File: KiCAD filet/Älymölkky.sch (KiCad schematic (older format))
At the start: 6 parts

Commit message: Added lots of new reference files and a new lib
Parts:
- removed U?: nRF52810-QCxx, Package_DFN_QFN:QFN-32-1EP_5x5mm_P0.5mm_EP3.6x3.6mm, symbol MCU_Nordic:nRF52810-QCxx
- added DEC1_C4, Vdd_nRF_C5: 100nF, symbol Device:C
- added L?: L, symbol Device:L
- added U?: nRF52810-QCxx, Package_DFN_QFN:QFN-32-1EP_5x5mm_P0.5mm_EP3.6x3.6mm, symbol MCU_Nordic_modified:nRF52810-QCxx
- added Vdd_nRF_C9: 4.7uF, symbol Device:C
- renumbered Vdd_nRF_C to Vdd_nRF_C8
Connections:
- net labels added: ANTENNA, LIS_INT1, VDD, ~CS, ~INT1, ~INT2, ~SAO_SDO, ~SCL_SPC, ~SDA_SDI
- net labels removed: Power_input_3.3V, Vdd, Vdd_IO, Vdd_nRF_input
- wire segments 37 -> 51
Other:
- note added: "Pin 32 to C9\nPin 25 to C8\nPin 9 to C5"
- moved on the sheet: Vdd_nRF_C8
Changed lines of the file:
@@
 EESchema Schematic File Version 4
+LIBS:Älymölkky-cache
 EELAYER 26 0
 EELAYER END
@@
 Wire Wire Line
 	7650 4750 7650 3350
-Text GLabel 8100 2750 0    50   Input ~ 0
-Power_input_3.3V
-Wire Wire Line
-	8250 2750 8100 2750
 Wire Wire Line
 	7650 3350 7950 3350
-Text Label 7950 3150 0    50   ~ 0
-Vdd_IO
 Wire Wire Line
 	7950 3000 8250 3000
@@
 Connection ~ 8950 4700
 Wire Wire Line
-	8950 4700 8950 5750
+	8950 4700 8950 5550
 Wire Wire Line
 	8200 4200 8200 3600
-Wire Wire Line
-	8200 3600 8500 3600
 Wire Wire Line
 	8500 3600 8500 2750
@@
 Connection ~ 8200 4200
 Connection ~ 8250 2750
-Text Label 8300 3600 0    50   ~ 0
-Vdd
-$Comp
-L MCU_Nordic:nRF52810-QCxx U?
-U 1 1 5C5B485F
-P 2850 5100
-F 0 "U?" H 2850 4014 50  0000 C CNN
-F 1 "nRF52810-QCxx" H 2850 3923 50  0000 C CNN
-F 2 "Package_DFN_QFN:QFN-32-1EP_5x5mm_P0.5mm_EP3.6x3.6mm" H 2850 3750 50  0001 C CNN
-F 3 "http://infocenter.nordicsemi.com/pdf/nRF52810_PS_v1.1.pdf" H 2350 5300 50  0001 C CNN
-	1    2850 5100
-	1    0    0    -1
-$EndComp
-$Comp
-L Device:C Vdd_nRF_C
+$Comp
+L Device:C Vdd_nRF_C8
 U 1 1 5C5B4866
-P 3250 3050
-F 0 "Vdd_nRF_C" H 3365 3096 50  0000 L CNN
-F 1 "100nF" H 3365 3005 50  0000 L CNN
-F 2 "" H 3250 3050 50  0001 C CNN
-F 3 "~" H 3250 3050 50  0001 C CNN
-	1    3250 3050
-	1    0    0    -1
-$EndComp
-Wire Wire Line
-	2850 4100 2850 2700
-Wire Wire Line
-	2850 2700 3100 2700
-$Comp
-L power:Earth #PWR?
-U 1 1 5C5B4870
-P 3250 3350
-F 0 "#PWR?" H 3250 3100 50  0001 C CNN
-F 1 "Earth" H 3250 3200 50  0001 C CNN
-F 2 "" H 3250 3350 50  0001 C CNN
-F 3 "~" H 3250 3350 50  0001 C CNN
-	1    3250 3350
-	1    0    0    -1
-$EndComp
-Text GLabel 3000 2300 0    50   Input ~ 0
-Vdd_nRF_input
-Wire Wire Line
-	3100 2700 3100 2300
-Wire Wire Line
-	3100 2300 3000 2300
-Connection ~ 3100 2700
-Wire Wire Line
-	3100 2700 3250 2700
+P 5200 3000
+F 0 "Vdd_nRF_C8" H 5315 3046 39  0000 L CNN
+F 1 "100nF" H 5315 2955 50  0000 L CNN
+F 2 "" H 5200 3000 50  0001 C CNN
+F 3 "~" H 5200 3000 50  0001 C CNN
+	1    5200 3000
+	1    0    0    -1
+$EndComp
 Wire Wire Line
 	8300 4200 8200 4200
@@
 Wire Wire Line
 	8950 3350 8950 3700
-Wire Wire Line
-	3250 2700 3250 2900
-Wire Wire Line
-	3250 3200 3250 3350
+Text Label 6750 6100 0    50   ~ 0
+LIS_INT1
+Text Label 7150 5050 2    50   ~ 0
+~CS
+Text Label 5950 4950 0    50   ~ 0
+~CS
+$Comp
+L Device:L L?
+U 1 1 5C5CAB8B
+P 6650 3900
+F 0 "L?" H 6703 3946 50  0000 L CNN
+F 1 "L" H 6703 3855 50  0000 L CNN
+F 2 "" H 6650 3900 50  0001 C CNN
+F 3 "~" H 6650 3900 50  0001 C CNN
+	1    6650 3900
+	1    0    0    -1
+$EndComp
+Wire Wire Line
+	5950 4600 5950 4550
+Wire Wire Line
+	6650 3750 6650 3600
+Text Label 6650 3600 0    50   ~ 0
+ANTENNA
+Wire Wire Line
+	8100 2750 8250 2750
+Wire Wire Line
+	8500 3600 8200 3600
+Text Label 7150 5150 2    50   ~ 0
+~SDA_SDI
+Text Label 5950 5050 0    50   ~ 0
+~SDA_SDI
+Text Label 7150 5250 2    50   ~ 0
+~SAO_SDO
+Text Label 5950 5150 0    50   ~ 0
+~SAO_SDO
+Text Label 7150 5350 2    50   ~ 0
+~SCL_SPC
+Text Label 5950 5250 0    50   ~ 0
+~SCL_SPC
+Text Label 8050 5150 0    50   ~ 0
+~INT1
+Text Label 5950 5450 0    50   ~ 0
+~INT1
+Text Label 8050 5250 0    50   ~ 0
+~INT2
+Text Label 5950 5550 0    50   ~ 0
+~INT2
+Wire Wire Line
+	8050 5550 8950 5550
+Connection ~ 8950 5550
+Wire Wire Line
+	8950 5550 8950 5750
+$Comp
+L Device:C Vdd_nRF_C9
+U 1 1 5C5D0DD8
+P 5800 3000
+F 0 "Vdd_nRF_C9" H 5915 3046 39  0000 L CNN
+F 1 "4.7uF" H 5915 2955 50  0000 L CNN
+F 2 "" H 5800 3000 50  0001 C CNN
+F 3 "~" H 5800 3000 50  0001 C CNN
+	1    5800 3000
+	1    0    0    -1
+$EndComp
+$Comp
+L Device:C Vdd_nRF_C5
+U 1 1 5C5D0E00
+P 6400 3000
+F 0 "Vdd_nRF_C5" H 6515 3046 39  0000 L CNN
+F 1 "100nF" H 6515 2955 50  0000 L CNN
+F 2 "" H 6400 3000 50  0001 C CNN
+F 3 "~" H 6400 3000 50  0001 C CNN
+	1    6400 3000
+	1    0    0    -1
+$EndComp
+Wire Wire Line
+	6650 4050 6650 4600
+Wire Wire Line
+	5950 4600 6650 4600
+Wire Wire Line
+	4550 4250 4550 3400
+Wire Wire Line
+	4550 3400 3750 3400
+Wire Wire Line
+	3750 3400 3750 3650
+$Comp
+L Device:C DEC1_C4
+U 1 1 5C5D43A2
+P 3750 3800
+F 0 "DEC1_C4" H 3865 3846 50  0000 L CNN
+F 1 "100nF" H 3865 3755 50  0000 L CNN
+F 2 "" H 3788 3650 50  0001 C CNN
+F 3 "~" H 3750 3800 50  0001 C CNN
+	1    3750 3800
+	1    0    0    -1
+$EndComp
+$Comp
+L power:VDD #PWR?
+U 1 1 5C5D4AF2
+P 5200 2800
+F 0 "#PWR?" H 5200 2650 50  0001 C CNN
+F 1 "VDD" H 5217 2973 50  0000 C CNN
+F 2 "" H 5200 2800 50  0001 C CNN
+F 3 "" H 5200 2800 50  0001 C CNN
+	1    5200 2800
+	1    0    0    -1
+$EndComp
+$Comp
+L power:VDD #PWR?
+U 1 1 5C5D4F0A
+P 8100 2750
+F 0 "#PWR?" H 8100 2600 50  0001 C CNN
+F 1 "VDD" H 8117 2923 50  0000 C CNN
+F 2 "" H 8100 2750 50  0001 C CNN
+F 3 "" H 8100 2750 50  0001 C CNN
+	1    8100 2750
+	1    0    0    -1
+$EndComp
+$Comp
+L power:Earth #PWR?
+U 1 1 5C5D52FB
+P 3750 3950
+F 0 "#PWR?" H 3750 3700 50  0001 C CNN
+F 1 "Earth" H 3750 3800 50  0001 C CNN
+F 2 "" H 3750 3950 50  0001 C CNN
+F 3 "~" H 3750 3950 50  0001 C CNN
+	1    3750 3950
+	1    0    0    -1
+$EndComp
+$Comp
+L MCU_Nordic_modified:nRF52810-QCxx U?
+U 1 1 5C5D854C
+P 5050 5250
+F 0 "U?" H 5050 4164 50  0000 C CNN
+F 1 "nRF52810-QCxx" H 5050 4073 50  0000 C CNN
+F 2 "Package_DFN_QFN:QFN-32-1EP_5x5mm_P0.5mm_EP3.6x3.6mm" H 5050 3900 50  0001 C CNN
+F 3 "http://infocenter.nordicsemi.com/pdf/nRF52810_PS_v1.1.pdf" H 4550 5450 50  0001 C CNN
+	1    5050 5250
+	1    0    0    -1
+$EndComp
+$Comp
+L power:Earth #PWR?
+U 1 1 5C5DA614
+P 5200 3150
+F 0 "#PWR?" H 5200 2900 50  0001 C CNN
+F 1 "Earth" H 5200 3000 50  0001 C CNN
+F 2 "" H 5200 3150 50  0001 C CNN
+F 3 "~" H 5200 3150 50  0001 C CNN
+	1    5200 3150
+	1    0    0    -1
+$EndComp
+Wire Wire Line
+	5050 2800 5200 2800
+Wire Wire Line
+	5200 2800 5200 2850
+Text Notes 6150 2400 0    50   ~ 0
+Pin 32 to C9\nPin 25 to C8\nPin 9 to C5
+Wire Wire Line
+	5250 4250 5250 3300
+Wire Wire Line
+	5250 3300 5700 3300
+Wire Wire Line
+	5700 3300 5700 2800
+Wire Wire Line
+	5700 2800 5800 2800
+Wire Wire Line
+	5800 2800 5800 2850
+Wire Wire Line
+	5350 4250 5350 3350
+Wire Wire Line
+	5350 3350 6300 3350
+Wire Wire Line
+	6300 3350 6300 2850
+Wire Wire Line
+	6300 2850 6400 2850
+Connection ~ 5200 2800
+$Comp
+L power:VDD #PWR?
+U 1 1 5C5DDF92
+P 5800 2800
+F 0 "#PWR?" H 5800 2650 50  0001 C CNN
+F 1 "VDD" H 5817 2973 50  0000 C CNN
+F 2 "" H 5800 2800 50  0001 C CNN
+F 3 "" H 5800 2800 50  0001 C CNN
+	1    5800 2800
+	1    0    0    -1
+$EndComp
+Connection ~ 5800 2800
+$Comp
+L power:VDD #PWR?
+U 1 1 5C5DDFD9
+P 6400 2850
+F 0 "#PWR?" H 6400 2700 50  0001 C CNN
+F 1 "VDD" H 6417 3023 50  0000 C CNN
+F 2 "" H 6400 2850 50  0001 C CNN
+F 3 "" H 6400 2850 50  0001 C CNN
+	1    6400 2850
+	1    0    0    -1
+$EndComp
+Connection ~ 6400 2850
+Wire Wire Line
+	5050 2800 5050 4300
 $EndSCHEMATC

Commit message: Removed redundant files and more cleanup
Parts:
- U?: symbol MCU_Nordic_modified:nRF52810-QCxx -> nrf52810-qcxx:nRF52810-QCxx
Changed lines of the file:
@@
 EESchema Schematic File Version 4
-LIBS:Älymölkky-cache
 EELAYER 26 0
 EELAYER END
@@
 $EndComp
 $Comp
-L MCU_Nordic_modified:nRF52810-QCxx U?
+L nrf52810-qcxx:nRF52810-QCxx U?
 U 1 1 5C5D854C
 P 5050 5250

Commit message: Added most of nrf52 pin connections
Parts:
- added DEC2_C6: N.C., symbol Device:C
- added DEC3_C7: 100pF, symbol Device:C
- added DEC4_C10: 1.0uF, symbol Device:C
- added U?: nRF52810-QCxx, Package_DFN_QFN:QFN-32-1EP_5x5mm_P0.5mm_EP3.6x3.6mm, symbol MCU_Nordic:nRF52810-QCxx
- added VSS_PIN20_C3: 0.8pF, symbol Device:C
- added X1, X2: 32MHz Crystal, symbol Device:Crystal
- added XC1_C1, XC2_C2, XL1_C11, XL2_C12: 12pF, symbol Device:C
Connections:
- net labels added: ~Reset, ~SWDCLK, ~SWDIO, ~VSS_PIN20
- net labels removed: LIS_INT1
- wire segments 51 -> 100
- no-connect marks 0 -> 8
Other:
- note added: "AIN0-AIN6+VDD/2 are multiplexer pins"
- note added: "OPTIONAL"
- note added: "Pin 29 (VSS) to DEC4 ground"
- moved on the sheet: L?

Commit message: Added comments on some pins
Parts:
- X2: value 32MHz Crystal -> 32.768 kHz Crystal
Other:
- note added: "For LIS2DE12:\nThe device core is supplied through the Vdd line\nwhile the I/O pads are supplied through the Vdd_IO line. \nPower supply decoupling capacitors (100 nF ceramic,\n 10 μF aluminum) should be placed as near as possible to\npin 9 of the device (common design practice).\n"
- note added: "Placeholder for antenna"
- note added: "SWDCLK and SWDIO are serial wire debug ports"
- note added: "VDD pins:\nPin 32 to C9\nPin 25 to C8\nPin 9 to C5"
- note added: "VSS pins:\nPin 20 to antenna ground\nPin 29 and 33 passive."
- note removed: "For LIS2DE12:\nThe device core is supplied through the Vdd line while the I/O pads are supplied through the\nVdd_IO line. Power supply decoupling capacitors (100 nF ceramic, 10 μF aluminum) should\nbe placed as near as possible to pin 9 of the device (common design practice).\n"
- note removed: "Pin 32 to C9\nPin 25 to C8\nPin 9 to C5"
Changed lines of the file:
@@
 $EndComp
 Text Notes 8950 2900 0    50   ~ 0
-For LIS2DE12:\nThe device core is supplied through the Vdd line while the I/O pads are supplied through the\nVdd_IO line. Power supply decoupling capacitors (100 nF ceramic, 10 μF aluminum) should\nbe placed as near as possible to pin 9 of the device (common design practice).\n
+For LIS2DE12:\nThe device core is supplied through the Vdd line\nwhile the I/O pads are supplied through the Vdd_IO line. \nPower supply decoupling capacitors (100 nF ceramic,\n 10 μF aluminum) should be placed as near as possible to\npin 9 of the device (common design practice).\n
 Wire Wire Line
 	7650 4750 7650 3350
@@
 Wire Wire Line
 	5200 2800 5200 2850
-Text Notes 6150 2400 0    50   ~ 0
-Pin 32 to C9\nPin 25 to C8\nPin 9 to C5
+Text Notes 5900 2550 0    50   ~ 0
+VDD pins:\nPin 32 to C9\nPin 25 to C8\nPin 9 to C5
 Wire Wire Line
 	5250 4250 5250 4050
@@
 	1    0    0    -1
 $EndComp
-Text Notes 5050 2100 0    50   ~ 0
+Text Notes 4950 2000 0    50   ~ 0
 Pin 29 (VSS) to DEC4 ground
 $Comp
@@
 P 6200 4000
 F 0 "X2" V 6154 4131 50  0000 L TNN
-F 1 "32MHz Crystal" V 6245 4131 50  0000 L CNN
+F 1 "32.768 kHz Crystal" V 6245 4131 50  0000 L CNN
 F 2 "" H 6200 4000 50  0001 C CNN
 F 3 "~" H 6200 4000 50  0001 C CNN
@@
 Text Label 3800 4650 0    50   ~ 0
 ~VSS_PIN20
-Text Label 5450 6350 0    50   ~ 0
+Text Label 5050 6050 0    50   ~ 0
 ~VSS_PIN20
 Wire Wire Line
@@
 NoConn ~ 5950 5350
 NoConn ~ 5950 5650
-Text Notes 6100 5800 0    39   ~ 0
+Text Notes 6050 5800 0    39   ~ 0
 AIN0-AIN6+VDD/2 are multiplexer pins
 NoConn ~ 5950 5750
@@
 $EndComp
 Connection ~ 6400 2800
+Text Notes 2950 6100 0    50   ~ 0
+SWDCLK and SWDIO are serial wire debug ports
+Text Notes 2500 4250 0    50   ~ 0
+Placeholder for antenna
+Text Notes 5450 6300 0    50   ~ 0
+VSS pins:\nPin 20 to antenna ground\nPin 29 and 33 passive.
 $EndSCHEMATC

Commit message: Added test points, leds and serial port programming pins
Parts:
- removed U?: nRF52810-QCxx, Package_DFN_QFN:QFN-32-1EP_5x5mm_P0.5mm_EP3.6x3.6mm, symbol MCU_Nordic:nRF52810-QCxx
- added CS_TP, GND_TP, INT1_TP, INT2_TP, P0.18_TP, RESET_TP, SAO_SDO_TP, SCL_SPC_TP, SDA_SDI_TP, SDWIO_TP, SWDCLK_TP, VDD_TP: Conn_01x01_Male, symbol Connector:Conn_01x01_Male
- added Coin_cell_battery: 3.3V, symbol Device:Battery_Cell
- added LED1, LED2: LED_ALT, symbol Device:LED_ALT
- added R_LED_1, R_LED_2: 220, symbol Device:R
- added Serial_program/debug: Conn_01x06_Male, symbol Connector:Conn_01x06_Male
- added Serial_wire_debug_interconnector: Conn_02x05_Odd_Even, symbol Connector_Generic:Conn_02x05_Odd_Even
- L1: renamed from L?; value L -> 3.9nH
- U: renamed from U?; symbol nrf52810-qcxx:nRF52810-QCxx -> nrf52810-custom:nRF52810-QCxx
- gave numbers to parts that had none: 1
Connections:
- net labels added: ~GND, ~P0.04, ~P0.05, ~P0.18, ~VDD
- wire segments 100 -> 137
- no-connect marks 8 -> 7
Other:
- note added: "AIN0-AIN6+VDD/2\nare multiplexer pins"
- note added: "LIS-NRF connections test points"
- note added: "Power and ground test points"
- note added: "Serial wire debug + reset test points"
- note removed: "AIN0-AIN6+VDD/2 are multiplexer pins"
- moved on the sheet: L1

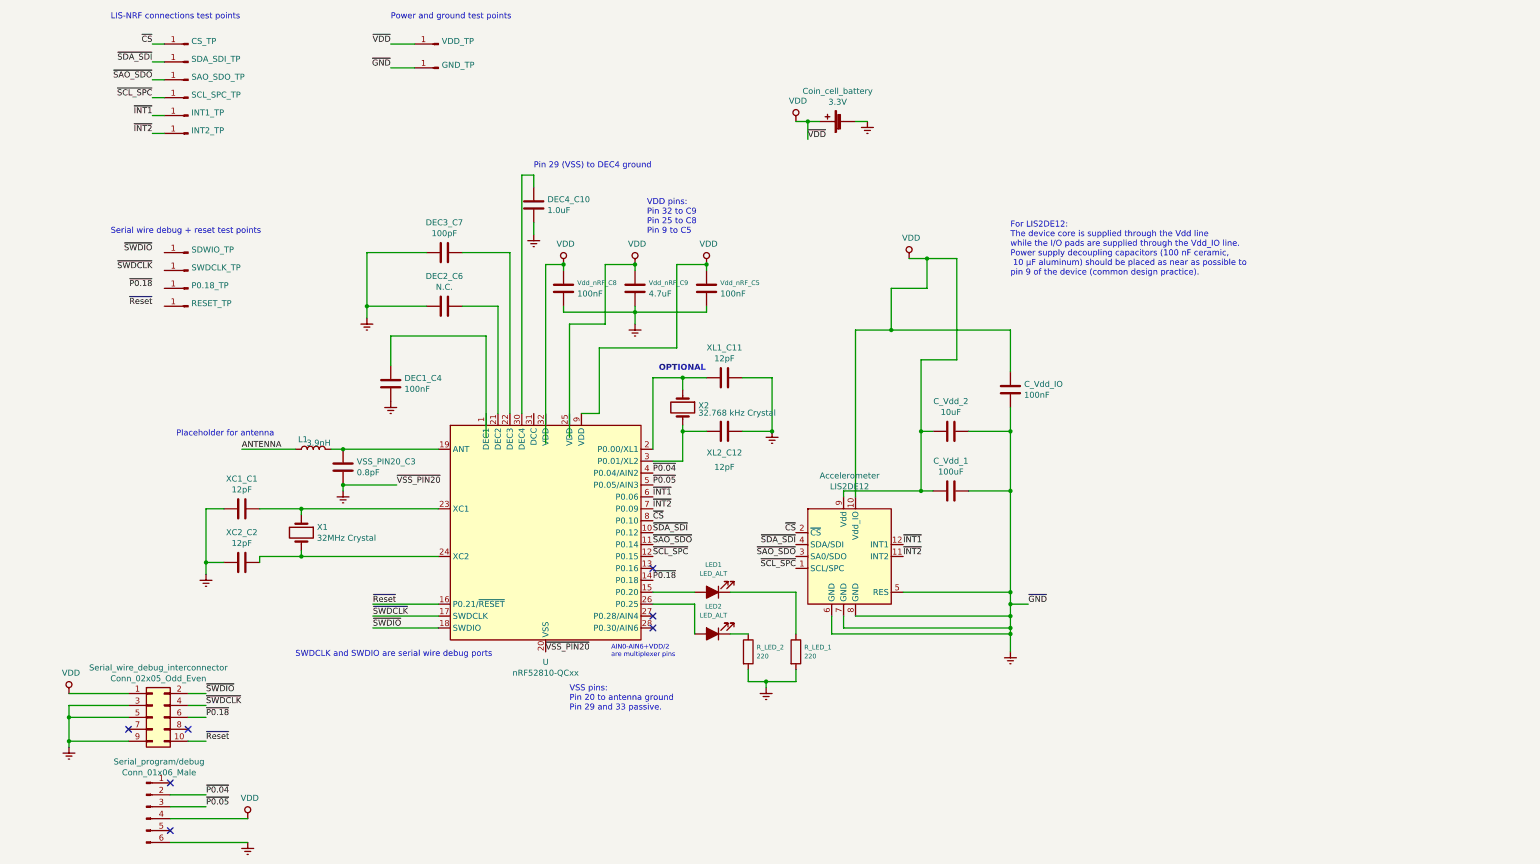
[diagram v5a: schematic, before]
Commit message: Added PCB component layouts
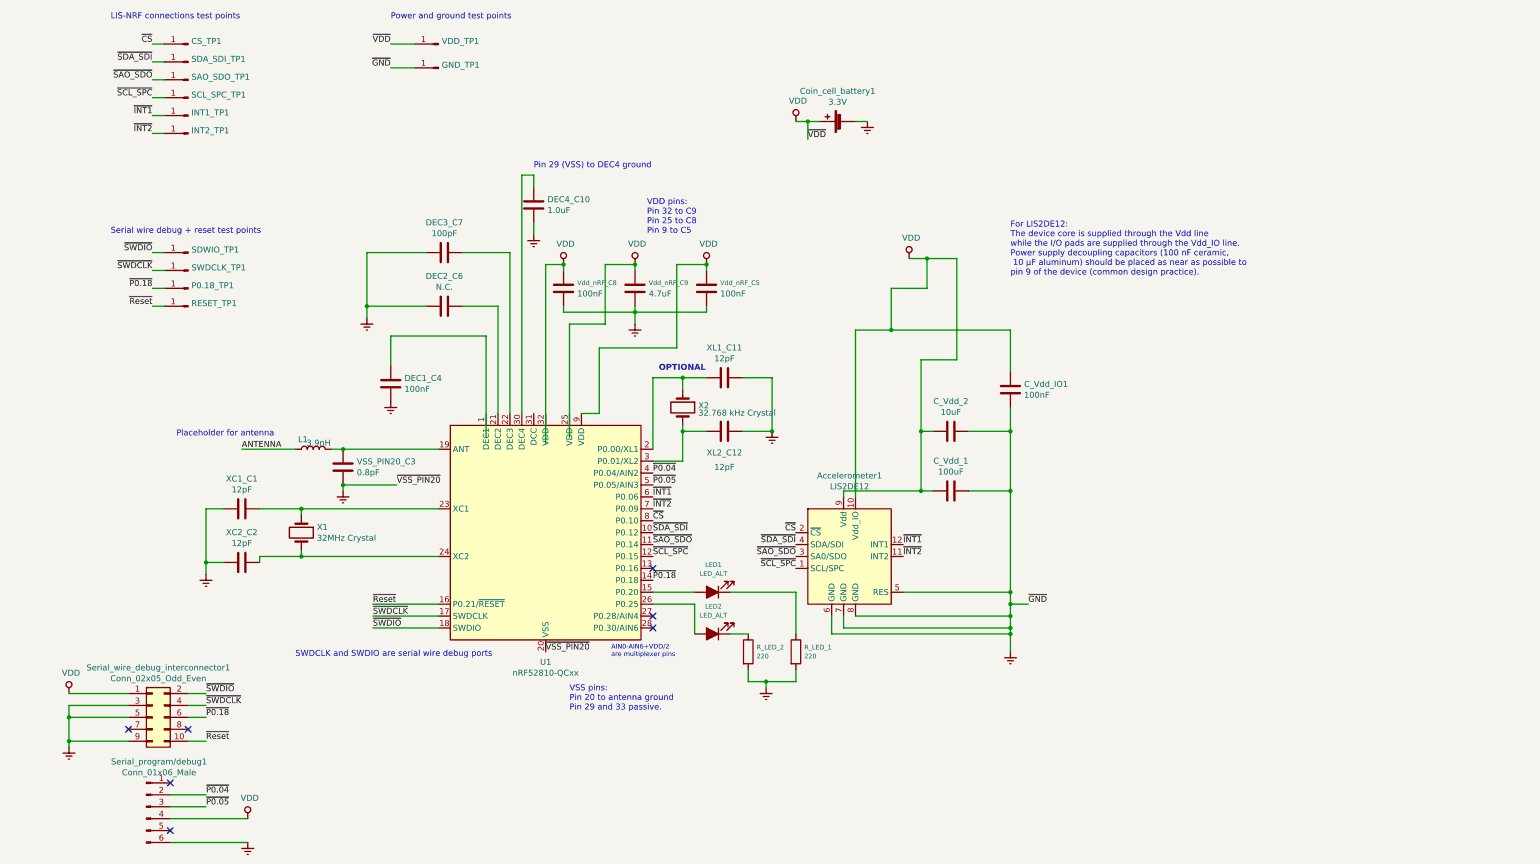
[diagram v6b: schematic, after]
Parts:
- CS_TP1: renamed from CS_TP; footprint (none) -> Connector_PinHeader_2.54mm:PinHeader_1x01_P2.54mm_Vertical
- C_Vdd_1, C_Vdd_2, DEC1_C4, DEC2_C6, DEC3_C7, DEC4_C10, Vdd_nRF_C5, Vdd_nRF_C8, Vdd_nRF_C9: footprint (none) -> Capacitor_SMD:C_0805_2012Metric_Pad1.15x1.40mm_HandSolder
- C_Vdd_IO1: renamed from C_Vdd_IO; footprint (none) -> Capacitor_SMD:C_0805_2012Metric_Pad1.15x1.40mm_HandSolder
- GND_TP1: renamed from GND_TP; footprint (none) -> Connector_PinHeader_2.54mm:PinHeader_1x01_P2.54mm_Vertical
- INT1_TP1: renamed from INT1_TP; footprint (none) -> Connector_PinHeader_2.54mm:PinHeader_1x01_P2.54mm_Vertical
- INT2_TP1: renamed from INT2_TP; footprint (none) -> Connector_PinHeader_2.54mm:PinHeader_1x01_P2.54mm_Vertical
- L1, LED1, LED2, R_LED_1, R_LED_2: footprint (none) -> Resistor_SMD:R_0805_2012Metric_Pad1.15x1.40mm_HandSolder
- P0.18_TP1: renamed from P0.18_TP; footprint (none) -> Connector_PinHeader_2.54mm:PinHeader_1x01_P2.54mm_Vertical
- RESET_TP1: renamed from RESET_TP; footprint (none) -> Connector_PinHeader_2.54mm:PinHeader_1x01_P2.54mm_Vertical
- SAO_SDO_TP1: renamed from SAO_SDO_TP; footprint (none) -> Connector_PinHeader_2.54mm:PinHeader_1x01_P2.54mm_Vertical
- SCL_SPC_TP1: renamed from SCL_SPC_TP; footprint (none) -> Connector_PinHeader_2.54mm:PinHeader_1x01_P2.54mm_Vertical
- SDA_SDI_TP1: renamed from SDA_SDI_TP; footprint (none) -> Connector_PinHeader_2.54mm:PinHeader_1x01_P2.54mm_Vertical
- SDWIO_TP1: renamed from SDWIO_TP; footprint (none) -> Connector_PinHeader_2.54mm:PinHeader_1x01_P2.54mm_Vertical
- SWDCLK_TP1: renamed from SWDCLK_TP; footprint (none) -> Connector_PinHeader_2.54mm:PinHeader_1x01_P2.54mm_Vertical
- Serial_program/debug1: renamed from Serial_program/debug; footprint (none) -> Connector_PinHeader_2.54mm:PinHeader_1x06_P2.54mm_Vertical
- Serial_wire_debug_interconnector1: renamed from Serial_wire_debug_interconnector; footprint (none) -> Connector_PinHeader_1.27mm:PinHeader_2x05_P1.27mm_Vertical_SMD
- VDD_TP1: renamed from VDD_TP; footprint (none) -> Connector_PinHeader_2.54mm:PinHeader_1x01_P2.54mm_Vertical
- renumbered Accelerometer to Accelerometer1, Coin_cell_battery to Coin_cell_battery1, U to U1
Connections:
- net ~P0.18: now also P0.18_TP1.1 (Pin_1)
- net ~Reset: now also RESET_TP1.1 (Pin_1)
- net ~SWDCLK: now also SWDCLK_TP1.1 (Pin_1)
- net ~SWDIO: now also SDWIO_TP1.1 (Pin_1)
